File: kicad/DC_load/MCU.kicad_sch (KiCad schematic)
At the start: 86 parts, among them J1 Conn_Coaxial, J6 USB_B, J7 Conn_01x06_Socket, J9 Conn_01x04_Socket, Q1 MMBT5401, SW1 RotaryEncoder_Switch, SW2 RotaryEncoder_Switch, SW3 SW_Push, SW8 SW_Push, U1 FSA3157P6X, U10 FSA3157P6X, U11 FSA3157P6X, U12 FSA3157P6X, U14 AMS1117-3.3, U15 74HC14D653, U16 LM4040DBZ-3, U17 CH340C, U2 Screen, U8 STM32F103C8Tx

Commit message: Oa.
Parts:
- removed J7: Conn_01x06_Socket, Connector_PinSocket_2.54mm:PinSocket_1x06_P2.54mm_Vertical, symbol Connector:Conn_01x06_Socket
- removed U16: LM4040DBZ-3, Package_TO_SOT_SMD:SOT-23, symbol Reference_Voltage:LM4040DBZ-3
- added C48, C49, C50, C51, C52: 100n, Capacitor_SMD:C_0603_1608Metric_Pad1.08x0.95mm_HandSolder, symbol Device:C
- added J8: Conn_01x05_Socket, Connector_PinSocket_2.54mm:PinSocket_1x05_P2.54mm_Vertical, symbol Connector:Conn_01x05_Socket
- added R56, R58: 10k, Resistor_SMD:R_0603_1608Metric_Pad0.98x0.95mm_HandSolder, symbol Device:R
- added R57: 49.9k, Resistor_SMD:R_0603_1608Metric_Pad0.98x0.95mm_HandSolder, symbol Device:R
- added U18: TL431DBZ, Package_TO_SOT_SMD:SOT-23, symbol Reference_Voltage:TL431DBZ
- C33: value 100n -> 10u; LCSC C14663 -> C96446
- J1: value Conn_Coaxial -> BNC
- J6: footprint Connector_USB:USB_B_OST_USB-B1HSxx_Horizontal -> DC_load:62910416121
- SW1, SW2: footprint DC_load:rotary_encoder_bottom_solder -> Rotary_Encoder:RotaryEncoder_Alps_EC11E-Switch_Vertical_H20mm
- U9: value ~ -> Front plate
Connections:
- net +3V3 is gone; now on net 3V3: J9.2 (Pin_2), R36.1, R37.1, R39.1, R41.1, R43.1, R45.1, R51.1, R54.1, R55.1, SW3.2
- net +5V: now also C33.1, R34.1; no longer R34.2
- net 3V3: now also C48.2, C49.2, C50.2, C51.2, C52.2, J8.3 (Pin_3)
- net CH1_PWM: now also U8.16 (PA6); no longer U8.29 (PA8)
- net CH2_PWM: now also U8.17 (PA7); no longer U8.38 (PA15)
- net CH3_PWM: now also U8.29 (PA8); no longer U8.16 (PA6)
- net CH4_PWM: now also U8.38 (PA15); no longer U8.17 (PA7)
- net CTRL_SEL: now also U8.15 (PA5)
- net ENC_A_1: now also U8.2 (PC13)
- net ENC_A_2: now also U8.27 (PB14)
- net ENC_B_1: now also U8.4 (PC15)
- net ENC_B_2: now also U8.28 (PB15)
- net ENC_SW_1: now also U8.3 (PC14)
- net ENC_SW_2: now also U8.20 (PB2)
- net GND: now also C33.2, C48.1, C49.1, C50.1, C51.1, C52.1, J8.5 (Pin_5), R57.2, R58.2, U18.3 (A); no longer C33.1
- net RX: now also J8.1 (Pin_1)
- net TX: now also J8.2 (Pin_2)
- net VREF: now also R34.2, R56.1, U18.1 (K); no longer C33.2, R34.1
- net at C35.1, D3.1 (K), Q1.1 (B): now also R58.1
- new net: R56.2, R57.1, U18.2 (REF)
- no-connect marks 5 -> 23
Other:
- moved on the sheet: C30, C31, C34, C35, C45, C47, D3, D4, Q1, R34, R35, R51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

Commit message: Most routing done.
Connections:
- net +5V is gone; now on net 5V: C31.1, C33.1, D4.2 (A), J6.1 (VBUS), R34.1, R35.2, U14.3 (VI)
- net ENC_A_2: now also U8.40 (PB4); no longer U8.27 (PB14)
- net ENC_B_2: now also U8.39 (PB3); no longer U8.28 (PB15)
- net ENC_SW_2: now also U8.41 (PB5); no longer U8.20 (PB2)
- net RX: no longer J8.1 (Pin_1), U8.30 (PA9)
- net TX: no longer J8.2 (Pin_2), U8.31 (PA10)
- net TX2: no longer names the net of R52.2, U8.12 (PA2)
- new net PROG_RX: J8.1 (Pin_1), U8.30 (PA9)
- new net PROG_TX: J8.2 (Pin_2), U8.31 (PA10)
- no-connect marks 23 -> 19
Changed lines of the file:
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@@
 		)
 	)
+	(text "STM_TX\n"
+		(exclude_from_sim no)
+		(at 313.436 161.798 0)
+		(effects
+			(font
+				(size 1.27 1.27)
+			)
+		)
+	)
 	(text "PWM DAC's and source mux"
 		(exclude_from_sim no)
@@
 		)
 	)
+	(text "STM_RX\n"
+		(exclude_from_sim no)
+		(at 313.69 164.084 0)
+		(effects
+			(font
+				(size 1.27 1.27)
+			)
+		)
+	)
 	(text "Voltage reference"
 		(exclude_from_sim no)
@@
 	)
 	(no_connect
-		(at 274.32 195.58)
-	)
-	(no_connect
 		(at 360.68 187.96)
 	)
@@
 	)
 	(no_connect
-		(at 274.32 198.12)
-	)
-	(no_connect
 		(at 274.32 167.64)
 	)
 	(no_connect
-		(at 309.88 193.04)
-	)
-	(no_connect
 		(at 215.9 167.64)
 	)
@@
 	)
 	(no_connect
-		(at 274.32 193.04)
-	)
-	(no_connect
 		(at 215.9 170.18)
 	)
@@
 	(wire
 		(pts
+			(xy 265.43 198.12) (xy 274.32 198.12)
+		)
+		(stroke
+			(width 0)
+			(type default)
+		)
+	)
+	(wire
+		(pts
 			(xy 67.31 194.31) (xy 67.31 196.85)
 		)
@@
 	(wire
 		(pts
+			(xy 264.16 195.58) (xy 274.32 195.58)
+		)
+		(stroke
+			(width 0)
+			(type default)
+		)
+	)
+	(wire
+		(pts
 			(xy 55.88 231.14) (xy 67.31 231.14)
 		)
@@
 	(wire
 		(pts
+			(xy 264.16 193.04) (xy 274.32 193.04)
+		)
+		(stroke
+			(width 0)
+			(type default)
+		)
+	)
+	(wire
+		(pts
 			(xy 86.36 71.12) (xy 90.17 71.12)
 		)
@@
 	(wire
 		(pts
+			(xy 317.5 193.04) (xy 309.88 193.04)
+		)
+		(stroke
+			(width 0)
+			(type default)
+		)
+	)
+	(wire
+		(pts
 			(xy 160.02 72.39) (xy 160.02 77.47)
 		)
@@
 		)
 	)
-	(label "TX"
-		(at 355.6 182.88 0)
+	(label "PROG_TX"
+		(at 347.98 182.88 0)
 		(effects
 			(font
@@
 		)
 	)
-	(label "RX"
-		(at 355.6 180.34 0)
+	(label "PROG_RX"
+		(at 347.98 180.34 0)
 		(effects
 			(font
@@
 		)
 	)
-	(label "TX2"
-		(at 311.15 162.56 0)
-		(effects
-			(font
-				(size 1.27 1.27)
-			)
-			(justify left bottom)
-		)
-	)
 	(global_label "ENC_B_1"
 		(shape input)
@@
 		)
 	)
-	(global_label "ENC_B_2"
-		(shape input)
-		(at 261.62 223.52 180)
-		(fields_autoplaced yes)
-		(effects
-			(font
-				(size 1.27 1.27)
-			)
-			(justify right)
-		)
-		(property "Intersheetrefs" "${INTERSHEET_REFS}"
-			(at 250.4706 223.52 0)
-			(effects
-				(font
-					(size 1.27 1.27)
-				)
-				(justify right)
-				(hide yes)
-			)
-		)
-	)
 	(global_label "CH4_PWM"
 		(shape input)
@@
 		)
 	)
-	(global_label "ENC_A_2"
+	(global_label "ENC_B_2"
 		(shape input)
-		(at 261.62 220.98 180)
+		(at 264.16 193.04 180)
 		(fields_autoplaced yes)
 		(effects
@@
 		)
 		(property "Intersheetrefs" "${INTERSHEET_REFS}"
-			(at 250.652 220.98 0)
+			(at 253.0106 193.04 0)
 			(effects
 				(font
@@
 		)
 	)
-	(global_label "ENC_SW_2"
-		(shape input)
-		(at 264.16 190.5 180)
-		(fields_autoplaced yes)
-		(effects
-			(font
-				(size 1.27 1.27)
-			)
-			(justify right)
-		)
-		(property "Intersheetrefs" "${INTERSHEET_REFS}"
-			(at 251.6197 190.5 0)
-			(effects
-				(font
-					(size 1.27 1.27)
-				)
-				(justify right)
-				(hide yes)
-			)
-		)
-	)
 	(global_label "CH2_CONTROL"
 		(shape output)
@@
 		)
 	)
+	(global_label "ENC_SW_2"
+		(shape input)
+		(at 265.43 198.12 180)
+		(fields_autoplaced yes)
+		(effects
+			(font
+				(size 1.27 1.27)
+			)
+			(justify right)
+		)
+		(property "Intersheetrefs" "${INTERSHEET_REFS}"
+			(at 252.8897 198.12 0)
+			(effects
+				(font
+					(size 1.27 1.27)
+				)
+				(justify right)
+				(hide yes)
+			)
+		)
+	)
 	(global_label "CH2_PWM"
 		(shape input)
@@
 		)
 	)
+	(global_label "ENC_A_2"
+		(shape input)
+		(at 264.16 195.58 180)
+		(fields_autoplaced yes)
+		(effects
+			(font
+				(size 1.27 1.27)
+			)
+			(justify right)
+		)
+		(property "Intersheetrefs" "${INTERSHEET_REFS}"
+			(at 253.192 195.58 0)
+			(effects
+				(font
+					(size 1.27 1.27)
+				)
+				(justify right)
+				(hide yes)
+			)
+		)
+	)
 	(global_label "SCL"
 		(shape output)
@@
 			)
 		)
-		(property "Value" "+5V"
+		(property "Value" "5V"
 			(at 191.77 21.59 0)
 			(effects
@@
 			)
 		)
-		(property "Value" "+5V"
+		(property "Value" "5V"
 			(at 325.12 41.91 0)
 			(effects
@@
 			)
 		)
-		(property "Value" "+5V"
+		(property "Value" "5V"
 			(at 161.29 144.78 0)
 			(effects
@@
 			)
 		)
-		(property "Value" "+5V"
+		(property "Value" "5V"
 			(at 213.36 21.59 0)
 			(effects
@@
 			)
 		)
-		(property "Value" "+5V"
+		(property "Value" "5V"
 			(at 254 43.18 0)
 			(effects

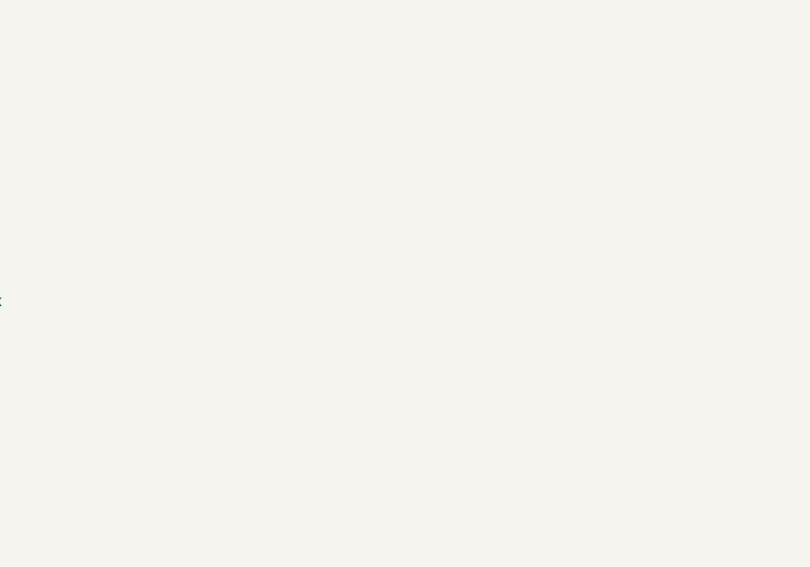
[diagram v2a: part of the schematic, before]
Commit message: Added EEPROM
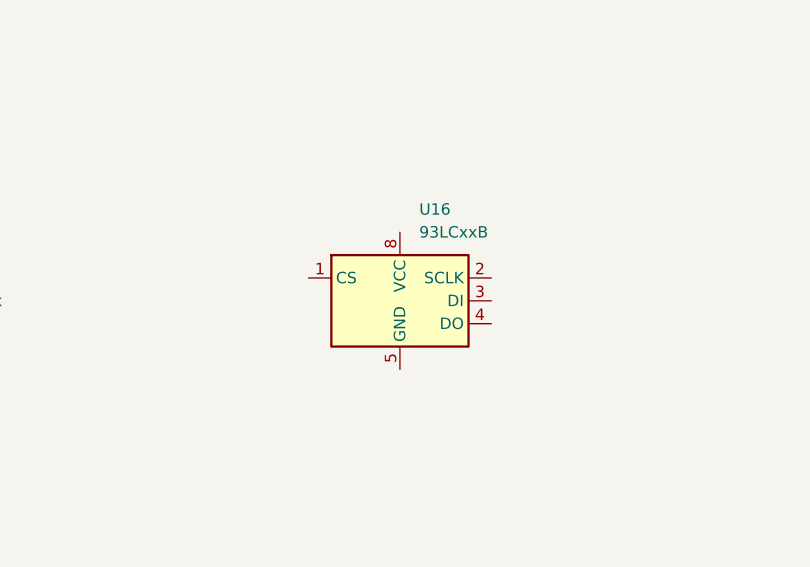
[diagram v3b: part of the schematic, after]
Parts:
- added U16: 93LCxxB, Package_SO:SOIC-8_3.9x4.9mm_P1.27mm, symbol Memory_EEPROM:93LCxxB
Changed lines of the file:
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@@
+	)
+	(symbol
+		(lib_id "Memory_EEPROM:93LCxxB")
+		(at 355.6 233.68 0)
+		(unit 1)
+		(exclude_from_sim no)
+		(in_bom yes)
+		(on_board yes)
+		(dnp no)
+		(fields_autoplaced yes)
+		(property "Reference" "U16"
+			(at 357.7433 223.52 0)
+			(effects
+				(font
+					(size 1.27 1.27)
+				)
+				(justify left)
+			)
+		)
+		(property "Value" "93LCxxB"
+			(at 357.7433 226.06 0)
+			(effects
+				(font
+					(size 1.27 1.27)
+				)
+				(justify left)
+			)
+		)
+		(property "Footprint" "Package_SO:SOIC-8_3.9x4.9mm_P1.27mm"
+			(at 355.6 233.68 0)
+			(effects
+				(font
+					(size 1.27 1.27)
+				)
+				(hide yes)
+			)
+		)
+		(property "Datasheet" "http://ww1.microchip.com/downloads/en/DeviceDoc/20001749K.pdf"
+			(at 355.6 233.68 0)
+			(effects
+				(font
+					(size 1.27 1.27)
+				)
+				(hide yes)
+			)
+		)
+		(property "Description" "Serial EEPROM, 93 Series, 2.5V, DIP-8/SOIC-8"
+			(at 355.6 233.68 0)
+			(effects
+				(font
+					(size 1.27 1.27)
+				)
+				(hide yes)
+			)
+		)
+		(pin "1"
+		)
+		(pin "7"
+		)
+		(pin "4"
+		)
+		(pin "3"
+		)
+		(pin "6"
+		)
+		(pin "5"
+		)
+		(pin "8"
+		)
+		(pin "2"
+		)
+		(instances
+			(project ""
+				(path "/ce255642-b081-42cc-af02-07a78c62b42e/57db3589-054f-4b81-a218-89ac743ece5d"
+					(reference "U16")
+					(unit 1)
+				)
+			)
+		)
 	)
 	(symbol

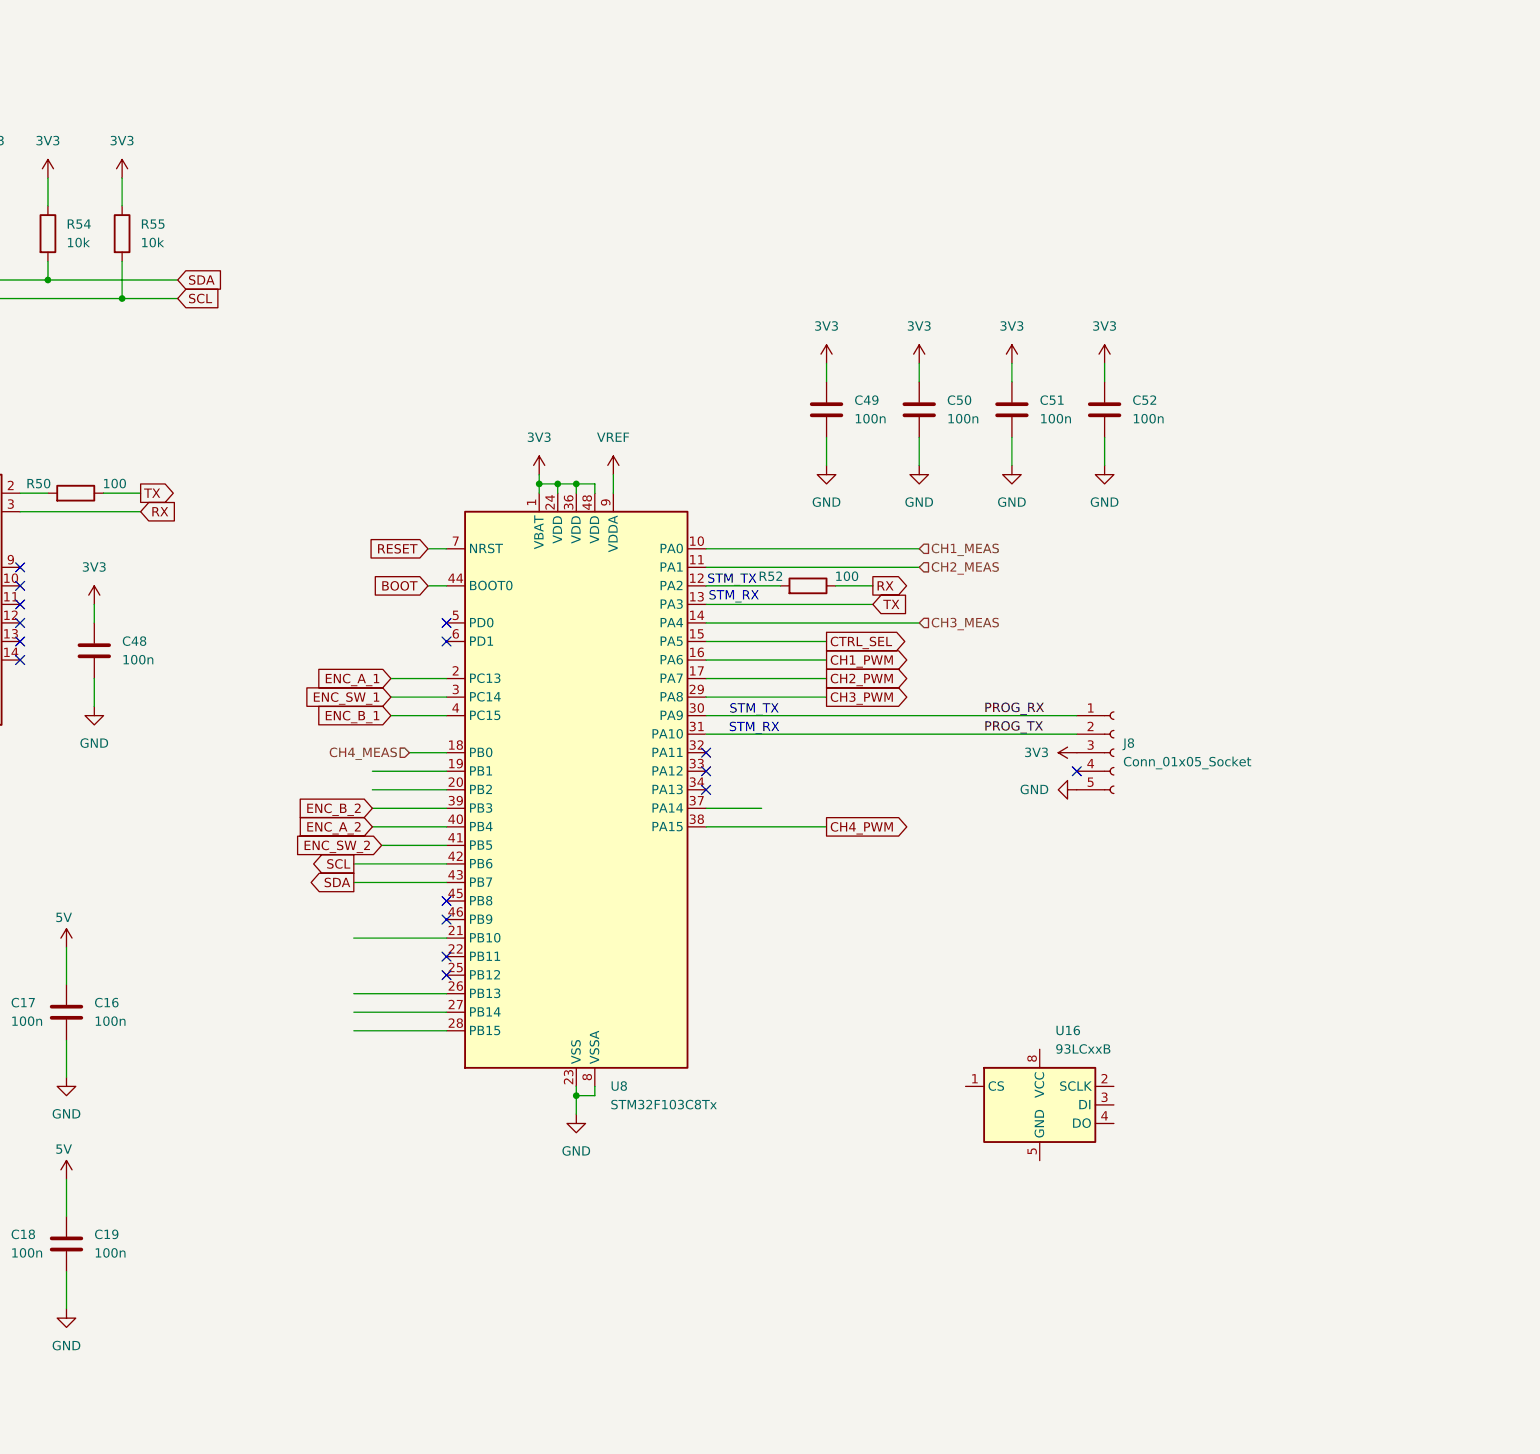
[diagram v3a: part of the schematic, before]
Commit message: MCU almost routed.
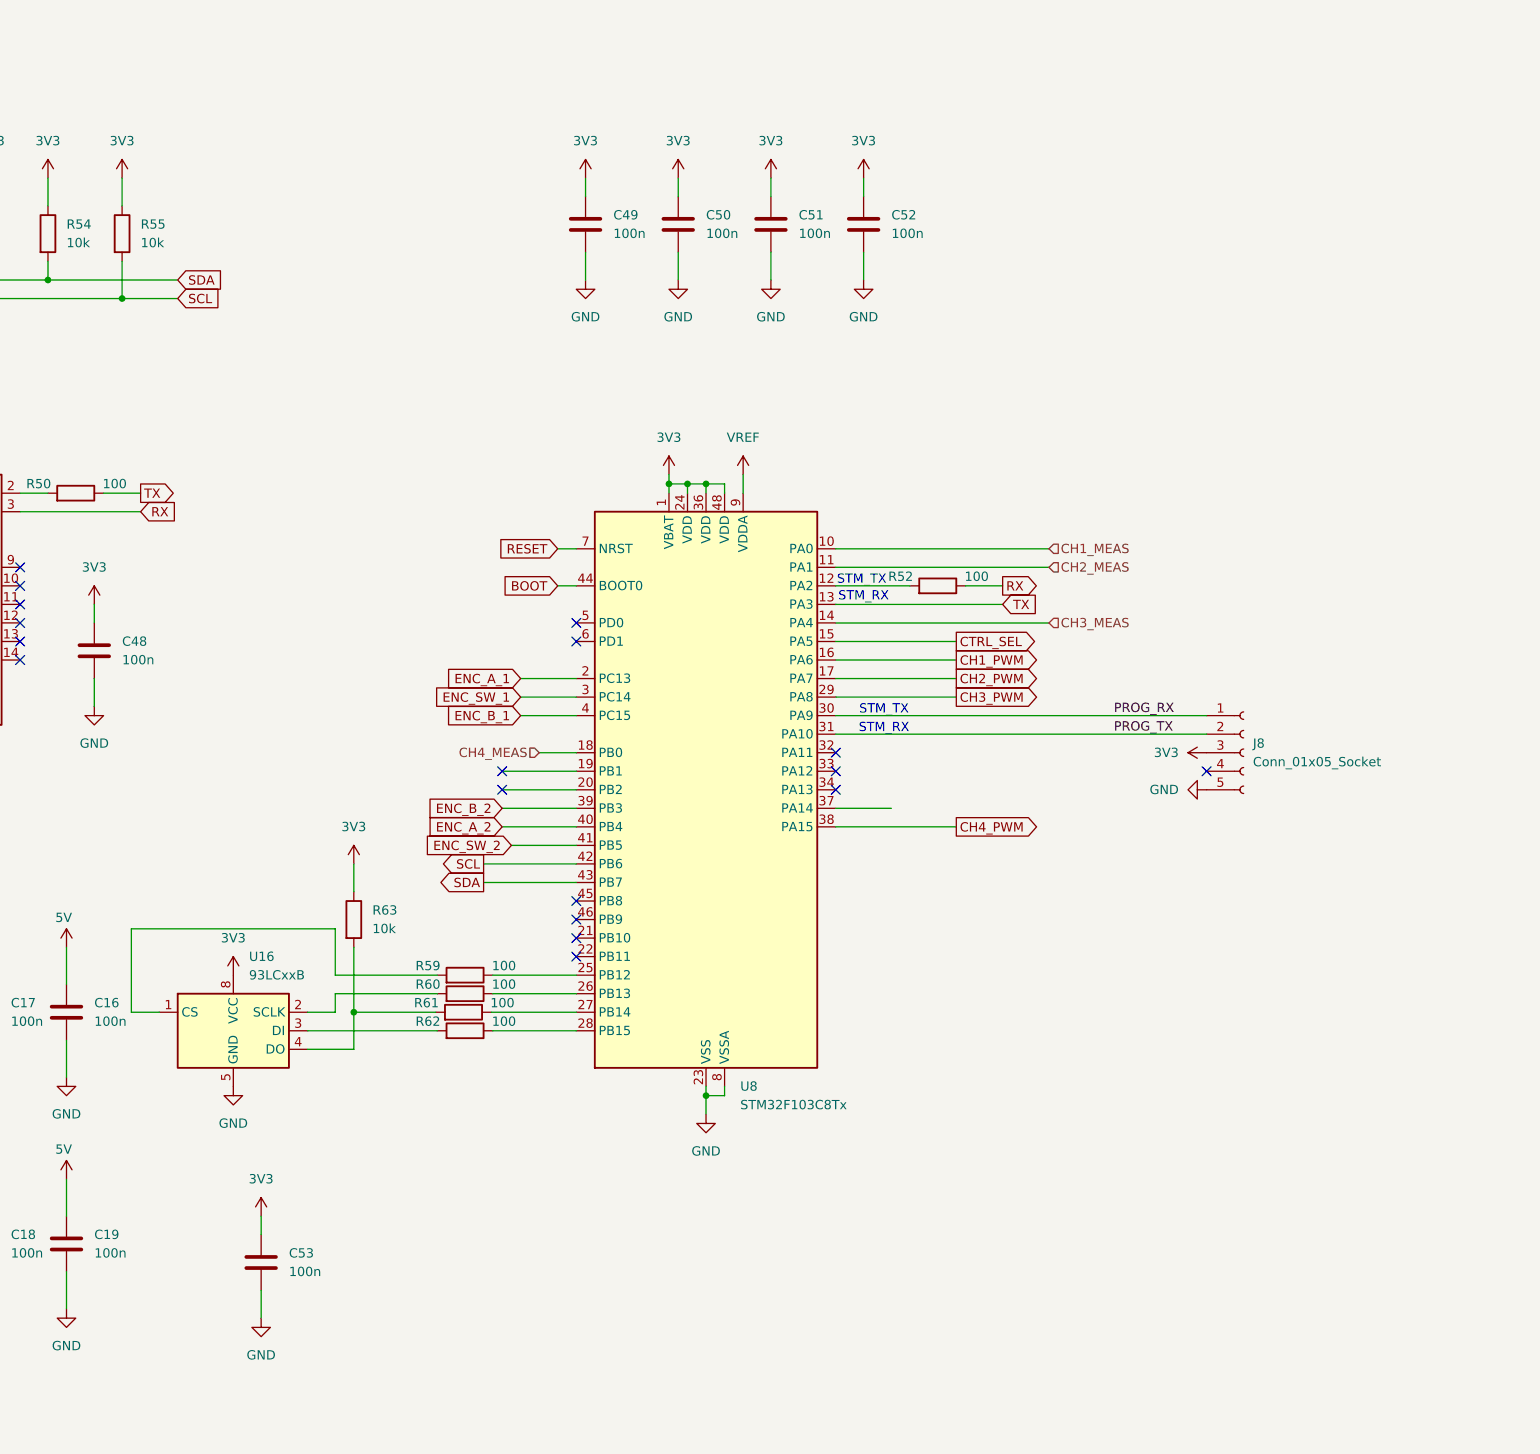
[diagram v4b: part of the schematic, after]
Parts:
- added C53: 100n, Capacitor_SMD:C_0603_1608Metric_Pad1.08x0.95mm_HandSolder, symbol Device:C
- added R59, R60, R61, R62: 100, Resistor_SMD:R_0603_1608Metric_Pad0.98x0.95mm_HandSolder, symbol Device:R
- added R63: 10k, Resistor_SMD:R_0603_1608Metric_Pad0.98x0.95mm_HandSolder, symbol Device:R
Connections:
- net 3V3: now also U16.8 (VCC), C53.2, R63.1
- net GND: now also U16.5 (GND), C53.1
- net at U16.1 (CS): now also R59.2
- net at U16.2 (SCLK): now also R60.2
- net at U16.3 (DI): now also R62.2
- net at U16.4 (DO): now also R61.2, R63.2
- net at U8.25 (PB12): now also R59.1
- net at U8.26 (PB13): now also R60.1
- net at U8.27 (PB14): now also R61.1
- net at U8.28 (PB15): now also R62.1
- no-connect marks 19 -> 21
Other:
- moved on the sheet: C49, C50, C51, C52, J8, R52, U16, U8

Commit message: All cool
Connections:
- net SINK_TEMP: now reaches U8.19 (PB1)
- no-connect marks 21 -> 20
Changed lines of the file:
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@@
 	)
 	(no_connect
-		(at 281.94 187.96)
-	)
-	(no_connect
 		(at 292.1 167.64)
 	)
@@
 	(wire
 		(pts
-			(xy 281.94 187.96) (xy 292.1 187.96)
+			(xy 104.14 59.69) (xy 118.11 59.69)
 		)
 		(stroke
@@
 	(wire
 		(pts
-			(xy 104.14 59.69) (xy 118.11 59.69)
+			(xy 185.42 179.07) (xy 185.42 181.61)
 		)
 		(stroke
@@
 	(wire
 		(pts
-			(xy 185.42 179.07) (xy 185.42 181.61)
+			(xy 29.21 215.9) (xy 29.21 219.71)
 		)
 		(stroke
@@
 	(wire
 		(pts
-			(xy 29.21 215.9) (xy 29.21 219.71)
+			(xy 80.01 250.19) (xy 82.55 250.19)
 		)
 		(stroke
@@
 	(wire
 		(pts
-			(xy 80.01 250.19) (xy 82.55 250.19)
+			(xy 440.69 73.66) (xy 440.69 77.47)
 		)
 		(stroke
@@
 	(wire
 		(pts
-			(xy 440.69 73.66) (xy 440.69 77.47)
+			(xy 287.02 187.96) (xy 292.1 187.96)
 		)
 		(stroke
@@
 		)
 	)
+	(hierarchical_label "SINK_TEMP"
+		(shape input)
+		(at 287.02 187.96 180)
+		(effects
+			(font
+				(size 1.27 1.27)
+			)
+			(justify right)
+		)
+	)
